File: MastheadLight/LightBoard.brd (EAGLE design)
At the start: 7.6 x 22.9 mm, 6 parts

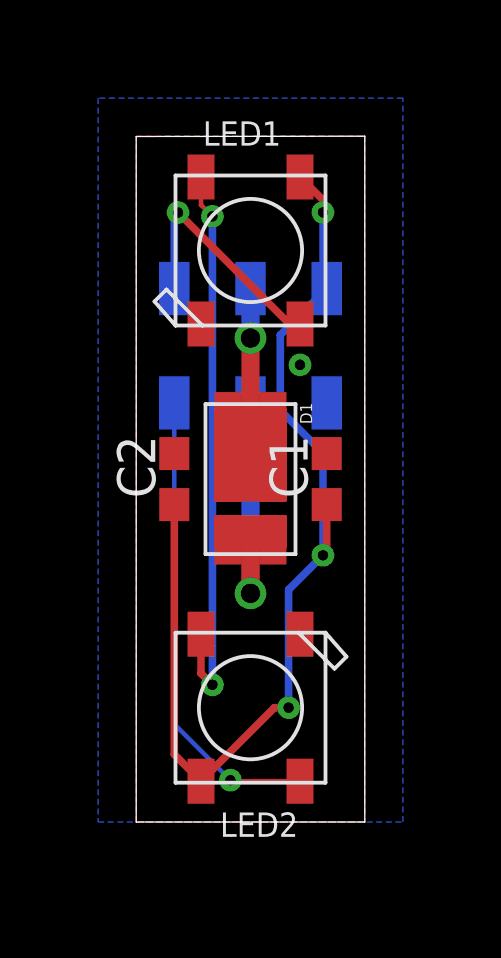
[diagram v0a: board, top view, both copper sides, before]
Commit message: Switched the light board to the proper six-pin WS2812B footprint.
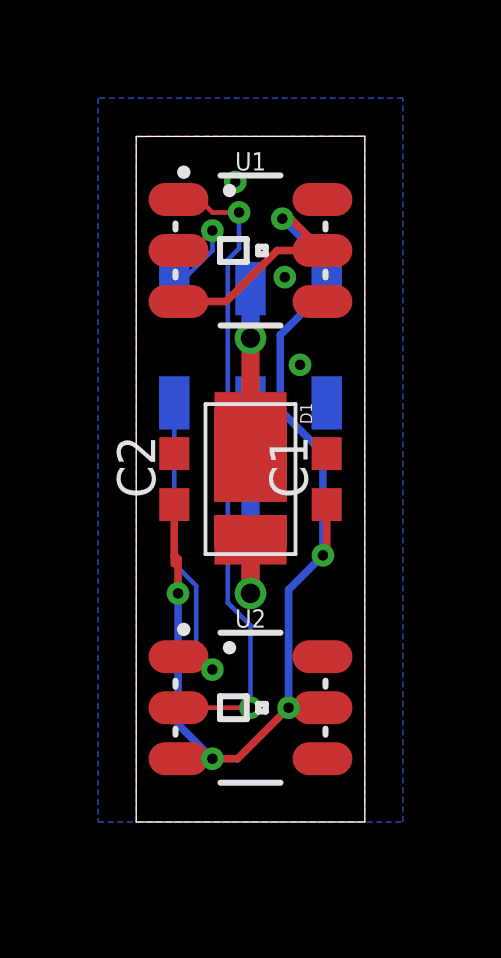
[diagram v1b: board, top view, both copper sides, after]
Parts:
- removed LED1, LED2: WS2812B5050, adafruit:WS2812B
- added U1, U2: WS2812, SparkFun-LED:LED-TRICOLOR-5050-IC
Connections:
- net +5V: now also U1.3, U1.5, U2.3, U2.5; no longer LED1.1-VDD, LED2.1-VDD
- net GND: now also U1.6, U2.6; no longer LED1.3-GND, LED2.3-GND
- net N$1: now also U1.1, U2.2; no longer LED1.2-DOUT, LED2.4-DIN
- net N$2: now also U1.2; no longer LED1.4-DIN
- net N$3: now also U2.1; no longer LED2.2-DOUT
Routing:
- net +5V: track 35.0 -> 42.6 mm, vias 3 -> 5
- net N$3: track 15.7 -> 10.7 mm
- net N$2: track 8.19 -> 3.86 mm
- net N$1: track 20.1 -> 21.6 mm
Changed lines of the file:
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@@
 </class>
 </classes>
-<designrules name="default">
+<designrules name="default *">
 <description language="de">&lt;b&gt;EAGLE Design Rules&lt;/b&gt;
 &lt;p&gt;
@@
 <param name="mlMinCreamFrame" value="0mil"/>
 <param name="mlMaxCreamFrame" value="0mil"/>
-<param name="mlViaStopLimit" value="0mil"/>
+<param name="mlViaStopLimit" value="15mil"/>
 <param name="srRoundness" value="0"/>
 <param name="srMinRoundness" value="0mil"/>
@@
 <element name="D1" library="PowerComponents" package="LM561C" value="LED" x="3.81" y="11.43" rot="R270"/>
 <element name="JP1" library="pinhead-1" package="2X03SMD/90" value="" x="2.54" y="8.89" rot="MR180"/>
-<element name="LED1" library="adafruit" library_urn="urn:adsk.eagle:library:420" package="WS2812B" value="WS2812B5050" x="3.81" y="19.05" rot="R90"/>
-<element name="LED2" library="adafruit" library_urn="urn:adsk.eagle:library:420" package="WS2812B" value="WS2812B5050" x="3.81" y="3.81" rot="R270"/>
+<element name="U1" library="SparkFun-LED" library_urn="urn:adsk.eagle:library:529" package="LED-TRICOLOR-5050-IC" package3d_urn="urn:adsk.eagle:package:39366/1" value="WS2812" x="3.81" y="19.05">
+<attribute name="PROD_ID" value="DIO-11598" x="3.81" y="19.05" size="1.778" layer="27" display="off"/>
+</element>
+<element name="U2" library="SparkFun-LED" library_urn="urn:adsk.eagle:library:529" package="LED-TRICOLOR-5050-IC" package3d_urn="urn:adsk.eagle:package:39366/1" value="WS2812" x="3.81" y="3.81">
+<attribute name="PROD_ID" value="DIO-11598" x="3.81" y="3.81" size="1.778" layer="27" display="off"/>
+</element>
 </elements>
 <signals>
-<signal name="N$1">
-<contactref element="LED1" pad="2-DOUT"/>
-<contactref element="LED2" pad="4-DIN"/>
-<via x="2.540171875" y="20.189134375" extent="1-16" drill="0.35"/>
-<wire x1="2.16" y1="6.86485625" x2="2.16" y2="6.26" width="0.254" layer="1"/>
-<wire x1="2.16" y1="21.5" x2="2.16" y2="20.56930625" width="0.1524" layer="1"/>
-<wire x1="2.16" y1="20.56930625" x2="2.540171875" y2="20.189134375" width="0.1524" layer="1"/>
-<wire x1="2.16" y1="6.26" x2="2.54" y2="5.88" width="0.1524" layer="1"/>
-<wire x1="2.16" y1="6.26" x2="2.16" y2="4.952" width="0.254" layer="1"/>
-<wire x1="2.16" y1="4.952" x2="2.54" y2="4.572" width="0.254" layer="1"/>
-<via x="2.54" y="4.572" extent="1-16" drill="0.35"/>
-<wire x1="2.54" y1="4.572" x2="2.540171875" y2="4.572171875" width="0.254" layer="16"/>
-<wire x1="2.540171875" y1="4.572171875" x2="2.540171875" y2="20.189134375" width="0.254" layer="16"/>
-</signal>
 <signal name="GND">
-<contactref element="LED1" pad="3-GND"/>
 <contactref element="C1" pad="2"/>
-<contactref element="LED2" pad="3-GND"/>
 <contactref element="C2" pad="2"/>
 <contactref element="JP1" pad="6"/>
@@
 </polygon>
 <via x="5.461" y="15.24" extent="1-16" drill="0.35"/>
+<contactref element="U1" pad="6"/>
+<contactref element="U2" pad="6"/>
+<via x="4.953" y="18.161" extent="1-16" drill="0.35"/>
+<via x="3.302" y="21.336" extent="1-16" drill="0.35"/>
 </signal>
 <signal name="+5V">
-<contactref element="LED1" pad="1-VDD"/>
 <contactref element="C1" pad="1"/>
-<contactref element="LED2" pad="1-VDD"/>
 <contactref element="C2" pad="1"/>
 <contactref element="JP1" pad="5"/>
-<wire x1="5.46" y1="21.5" x2="6.2258" y2="20.7342" width="0.254" layer="1"/>
-<wire x1="6.2258" y1="20.7342" x2="6.2258" y2="20.32" width="0.254" layer="1"/>
-<via x="6.2258" y="20.32" extent="1-16" drill="0.35"/>
-<wire x1="6.2258" y1="20.32" x2="6.2258" y2="17.9042" width="0.254" layer="16"/>
-<wire x1="6.2258" y1="17.9042" x2="6.35" y2="17.78" width="0.254" layer="16"/>
-<wire x1="1.27" y1="10.58" x2="1.27" y2="2.25" width="0.254" layer="1"/>
-<wire x1="1.27" y1="2.25" x2="2.16" y2="1.36" width="0.254" layer="1"/>
+<wire x1="1.27" y1="10.58" x2="1.27" y2="8.89" width="0.254" layer="1"/>
+<wire x1="1.27" y1="8.89" x2="1.27" y2="8.6" width="0.254" layer="1"/>
 <wire x1="6.35" y1="10.58" x2="6.35" y2="9.0142" width="0.254" layer="1"/>
 <wire x1="6.35" y1="9.0142" x2="6.2258" y2="8.89" width="0.254" layer="1"/>
@@
 <wire x1="4.8034" y1="13.72446875" x2="4.8034" y2="16.2334" width="0.254" layer="16"/>
 <wire x1="4.8034" y1="16.2334" x2="6.35" y2="17.78" width="0.254" layer="16"/>
-<wire x1="2.16" y1="1.36" x2="4.61" y2="3.81" width="0.254" layer="1"/>
-<wire x1="4.61" y1="3.81" x2="5.08" y2="3.81" width="0.254" layer="1"/>
+<wire x1="5.08" y1="7.7442" x2="6.2258" y2="8.89" width="0.254" layer="16"/>
+<contactref element="U1" pad="5"/>
+<contactref element="U1" pad="3"/>
+<contactref element="U2" pad="5"/>
+<contactref element="U2" pad="3"/>
+<wire x1="1.41" y1="17.35" x2="2.999" y2="17.35" width="0.254" layer="1"/>
+<wire x1="4.699" y1="19.05" x2="2.999" y2="17.35" width="0.254" layer="1"/>
+<wire x1="1.41" y1="2.11" x2="2.54" y2="2.11" width="0.254" layer="1"/>
+<wire x1="2.54" y1="2.11" x2="3.38" y2="2.11" width="0.254" layer="1"/>
+<wire x1="3.38" y1="2.11" x2="5.08" y2="3.81" width="0.254" layer="1"/>
 <via x="5.08" y="3.81" extent="1-16" drill="0.35"/>
 <wire x1="5.08" y1="3.81" x2="5.08" y2="7.7442" width="0.254" layer="16"/>
-<wire x1="5.08" y1="7.7442" x2="6.2258" y2="8.89" width="0.254" layer="16"/>
+<wire x1="6.21" y1="3.81" x2="5.08" y2="3.81" width="0.254" layer="1"/>
+<wire x1="1.27" y1="8.89" x2="1.3942" y2="8.7658" width="0.254" layer="1"/>
+<wire x1="1.3942" y1="8.7658" x2="1.3942" y2="7.62" width="0.254" layer="1"/>
+<via x="1.3942" y="7.62" extent="1-16" drill="0.35"/>
+<wire x1="1.3942" y1="7.62" x2="1.3942" y2="3.2558" width="0.254" layer="16"/>
+<wire x1="1.3942" y1="3.2558" x2="2.54" y2="2.11" width="0.254" layer="16"/>
+<via x="2.54" y="2.11" extent="1-16" drill="0.35"/>
+<wire x1="6.21" y1="19.05" x2="4.699" y2="19.05" width="0.254" layer="1"/>
+<wire x1="6.35" y1="17.78" x2="6.21" y2="17.92" width="0.254" layer="16"/>
+<wire x1="6.21" y1="19.05" x2="5.1491" y2="20.1109" width="0.254" layer="1"/>
+<wire x1="5.1491" y1="20.1109" x2="4.8709" y2="20.1109" width="0.254" layer="1"/>
+<via x="4.8709" y="20.1109" extent="1-16" drill="0.35"/>
+<wire x1="4.8709" y1="20.1109" x2="6.35" y2="18.6318" width="0.254" layer="16"/>
+<wire x1="6.35" y1="18.6318" x2="6.35" y2="17.78" width="0.254" layer="16"/>
 </signal>
 <signal name="N$2">
-<contactref element="LED1" pad="4-DIN"/>
 <contactref element="JP1" pad="1"/>
-<wire x1="1.27" y1="17.78" x2="1.27" y2="20.19121875" width="0.254" layer="16"/>
-<wire x1="1.27" y1="20.19121875" x2="1.3942" y2="20.31541875" width="0.254" layer="16"/>
-<via x="1.3942" y="20.31541875" extent="1-16" drill="0.35"/>
-<wire x1="1.3942" y1="20.31541875" x2="5.10961875" y2="16.6" width="0.254" layer="1"/>
-<wire x1="5.10961875" y1="16.6" x2="5.46" y2="16.6" width="0.254" layer="1"/>
+<contactref element="U1" pad="2" route="any" routetag="U1.DI"/>
+<wire x1="1.41" y1="19.05" x2="1.8768" y2="19.05" width="0.1524" layer="1"/>
+<wire x1="1.8768" y1="19.05" x2="2.54" y2="19.7132" width="0.1524" layer="1"/>
+<via x="2.54" y="19.7132" extent="1-16" drill="0.35"/>
+<wire x1="2.54" y1="19.7132" x2="2.54" y2="19.05" width="0.1524" layer="16"/>
+<wire x1="2.54" y1="19.05" x2="1.27" y2="17.78" width="0.1524" layer="16"/>
 </signal>
 <signal name="N$3">
 <contactref element="JP1" pad="2"/>
-<contactref element="LED2" pad="2-DOUT"/>
-<wire x1="1.27" y1="13.97" x2="1.27" y2="3.2648" width="0.1524" layer="16"/>
-<wire x1="1.27" y1="3.2648" x2="3.1406" y2="1.3942" width="0.1524" layer="16"/>
-<via x="3.1406" y="1.3942" extent="1-16" drill="0.35"/>
-<wire x1="3.1406" y1="1.3942" x2="3.1748" y2="1.36" width="0.1524" layer="1"/>
-<wire x1="3.1748" y1="1.36" x2="5.46" y2="1.36" width="0.1524" layer="1"/>
+<contactref element="U2" pad="1"/>
+<via x="2.54" y="5.08" extent="1-16" drill="0.35"/>
+<wire x1="1.27" y1="13.97" x2="1.27" y2="8.60235" width="0.1524" layer="16"/>
+<wire x1="1.27" y1="8.60235" x2="2.001" y2="7.87135" width="0.1524" layer="16"/>
+<wire x1="2.001" y1="5.619" x2="2.54" y2="5.08" width="0.1524" layer="16"/>
+<wire x1="2.001" y1="7.87135" x2="2.001" y2="5.619" width="0.1524" layer="16"/>
+<wire x1="1.41" y1="5.51" x2="2.11" y2="5.51" width="0.1524" layer="1"/>
+<wire x1="2.11" y1="5.51" x2="2.54" y2="5.08" width="0.1524" layer="1"/>
 </signal>
 <signal name="N$5">
@@
 <wire x1="3.335" y1="12.23" x2="3.06" y2="12.505" width="0.6096" layer="1"/>
 </signal>
+<signal name="N$1">
+<contactref element="U1" pad="1"/>
+<contactref element="U2" pad="2" route="any" routetag="U1.DI"/>
+<wire x1="1.41" y1="3.81" x2="3.81" y2="3.81" width="0.1524" layer="1"/>
+<via x="3.81" y="3.81" extent="1-16" drill="0.35"/>
+<via x="3.429" y="20.32" extent="1-16" drill="0.35"/>
+<wire x1="3.81" y1="3.81" x2="3.81" y2="6.54971875" width="0.1524" layer="16"/>
+<wire x1="3.429" y1="19.1192875" x2="3.429" y2="20.32" width="0.1524" layer="16"/>
+<wire x1="3.81" y1="6.54971875" x2="3.0532" y2="7.30651875" width="0.1524" layer="16"/>
+<wire x1="3.0532" y1="18.7434875" x2="3.429" y2="19.1192875" width="0.1524" layer="16"/>
+<wire x1="3.0532" y1="7.30651875" x2="3.0532" y2="18.7434875" width="0.1524" layer="16"/>
+<wire x1="2.54" y1="20.32" x2="3.429" y2="20.32" width="0.1524" layer="1"/>
+<wire x1="1.41" y1="20.75" x2="2.11" y2="20.75" width="0.1524" layer="1"/>
+<wire x1="2.11" y1="20.75" x2="2.54" y2="20.32" width="0.1524" layer="1"/>
+</signal>
 </signals>

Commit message: As per Dec 2019 board orders
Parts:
- removed U1, U2: WS2812, SparkFun-LED:LED-TRICOLOR-5050-IC
- added D2, D3: WS2812B, SparkFun-LED:WS2812B
- turned C1 to 270 degrees
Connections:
- net +5V: now also D2.1, D3.1; no longer U1.3, U1.5, U2.3, U2.5
- net GND: now also D2.3, D3.3; no longer U1.6, U2.6
- net N$1: now also D2.2, D3.4; no longer U1.1, U2.2
- net N$2: now also D2.4; no longer U1.2
- net N$3: now also D3.2; no longer U2.1
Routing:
- net +5V: track 42.6 -> 29.1 mm, vias 5 -> 3
- net N$1: track 21.6 -> 19.5 mm
- net N$3: track 10.7 -> 11.9 mm
